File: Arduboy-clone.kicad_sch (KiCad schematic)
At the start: 0 parts

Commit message: Added MPU, Display and Decoupling Capacitors
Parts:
- added C? (x6): 0.1uF, Capacitor_SMD:C_0201_0603Metric, symbol PCM_SparkFun-Capacitor:0.1uF_0402_16V_10%
- added C? (x2): 22pF, PCM_SparkFun-Capacitor:C_0603_1608Metric, symbol PCM_SparkFun-Capacitor:C
- added C? (x2): 4.7uF, Capacitor_SMD:C_0201_0603Metric, symbol PCM_SparkFun-Capacitor:0.1uF_0402_16V_10%
- added C? (x3): 1uF, Capacitor_SMD:C_0201_0603Metric, symbol PCM_SparkFun-Capacitor:0.1uF_0402_16V_10%
- added R? (x2): 22k, PCM_SparkFun-Resistor:R_0402_1005Metric, symbol PCM_SparkFun-Resistor:22k_0402
- added R? (x2): 10k, PCM_SparkFun-Resistor:R_0402_1005Metric, symbol PCM_SparkFun-Resistor:10k_0402
- added SW? (x6): SW_Push, symbol Switch:SW_Push
- added U1: ATmega32U4-A, Package_QFP:TQFP-44_10x10mm_P0.8mm, symbol MCU_Microchip_ATmega:ATmega32U4-A
- added U?: OLED_1.3in, PCM_SparkFun-Display:OLED_1.3in_128x64-Folded, symbol PCM_SparkFun-Display:OLED_1.3in
- added Y1: 16MHz, PCM_SparkFun-Clock:Crystal_SMD_2.0x1.6mm, symbol PCM_SparkFun-Clock:Crystal_16MHz_2.0x1.6mm
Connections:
- new net: C?.1, U?.2 (C2P)
- new net: C?.1, U?.27 (VCOMH)
- new net: C?.1, U?.28 (VCC)
- new net: C?.2, U?.3 (C2N)
- new net: C?.2, U?.4 (C1P)
- new net: C?.1, U?.5 (C1N)
- new net: SW?.1, U1.39 (PF4)
- new net: R?.2, U1.4 (D+)
- new net: R?.1, U1.33 (~{HWB}/PE2)
- new net: C?.1, U1.16 (XTAL2), Y1.1
- new net: SW?.1, U1.36 (PF7)
- new net: C?.2, U1.6 (UCAP)
- new net: SW?.1, U1.1 (PE6)
- new net: SW?.1, U1.37 (PF6)
- new net: C?.2, U1.17 (XTAL1), Y1.2
- new net: SW?.1, U1.28 (PB4)
- new net: R?.2, U1.3 (D-)
- new net: SW?.1, U1.38 (PF5)
- new net 5V: C?.1, C?.1, C?.1, C?.1, C?.1, C?.1, U1.14 (VCC), U1.2 (UVCC), U1.24 (AVCC), U1.34 (VCC), U1.44 (AVCC), U?.6 (VDDB), U?.9 (VDD)
- new net CLK: U1.9 (PB1), U?.18 (D0/SCK/SCL)
- new net CS: U1.27 (PD7), U?.13 (~{CS})
- new net DC: U1.25 (PD4), U?.15 (D/~{C})
- new net GND: C?.1, C?.1, C?.2, C?.2, C?.2, C?.2, C?.2, C?.2, C?.2, C?.2, C?.2, R?.2, R?.2, SW?.2, SW?.2, SW?.2, SW?.2, SW?.2, SW?.2, U1.15 (GND), U1.23 (GND), U1.35 (GND), U1.43 (GND), U1.5 (UGND), U?.1 (GND), U?.10 (BS0), U?.11 (BS1), U?.12 (BS2), U?.16 (R/~{W}), U?.17 (E/~{RD}), U?.20 (D2/SDA), U?.21 (D3), U?.22 (D4), U?.23 (D5), U?.24 (D6), U?.29 (VLSS), U?.30 (GND), U?.8 (VSS)
- new net MOSI: U1.10 (PB2), U?.19 (D1/MOSI/SDA)
- new net RES: U1.31 (PC6), U?.14 (~{RESET})
- new net RESET: R?.1, U1.13 (~{RESET})
- new net USB_D+: R?.1
- new net USB_D-: R?.1

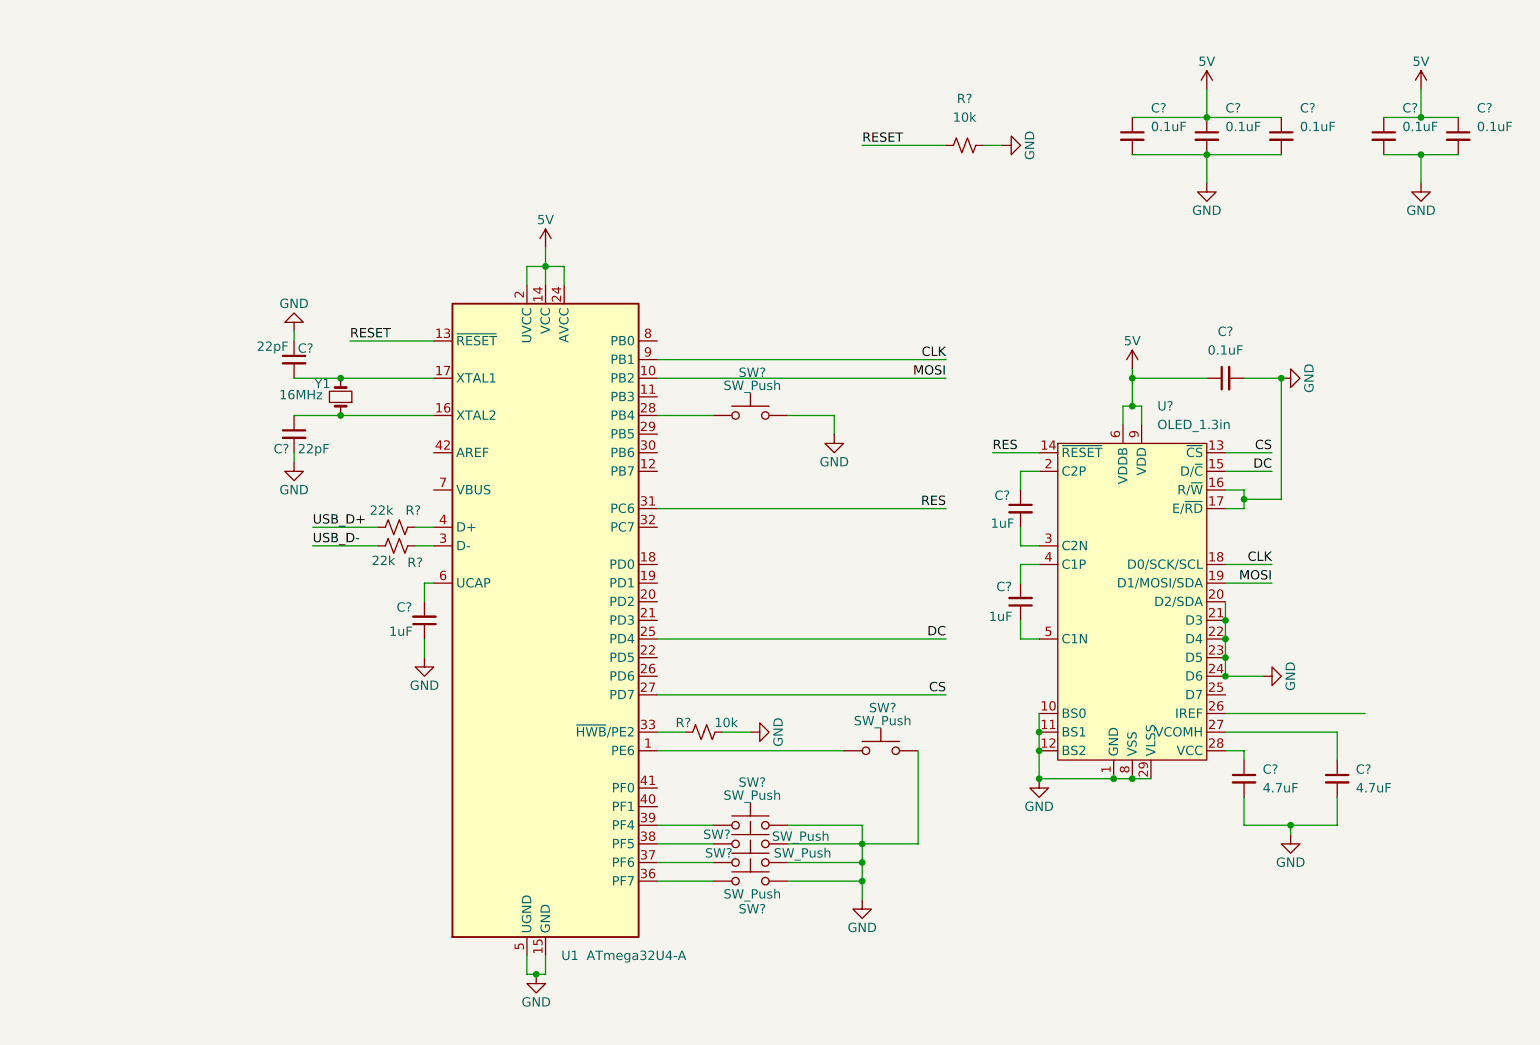
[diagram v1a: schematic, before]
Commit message: added display header
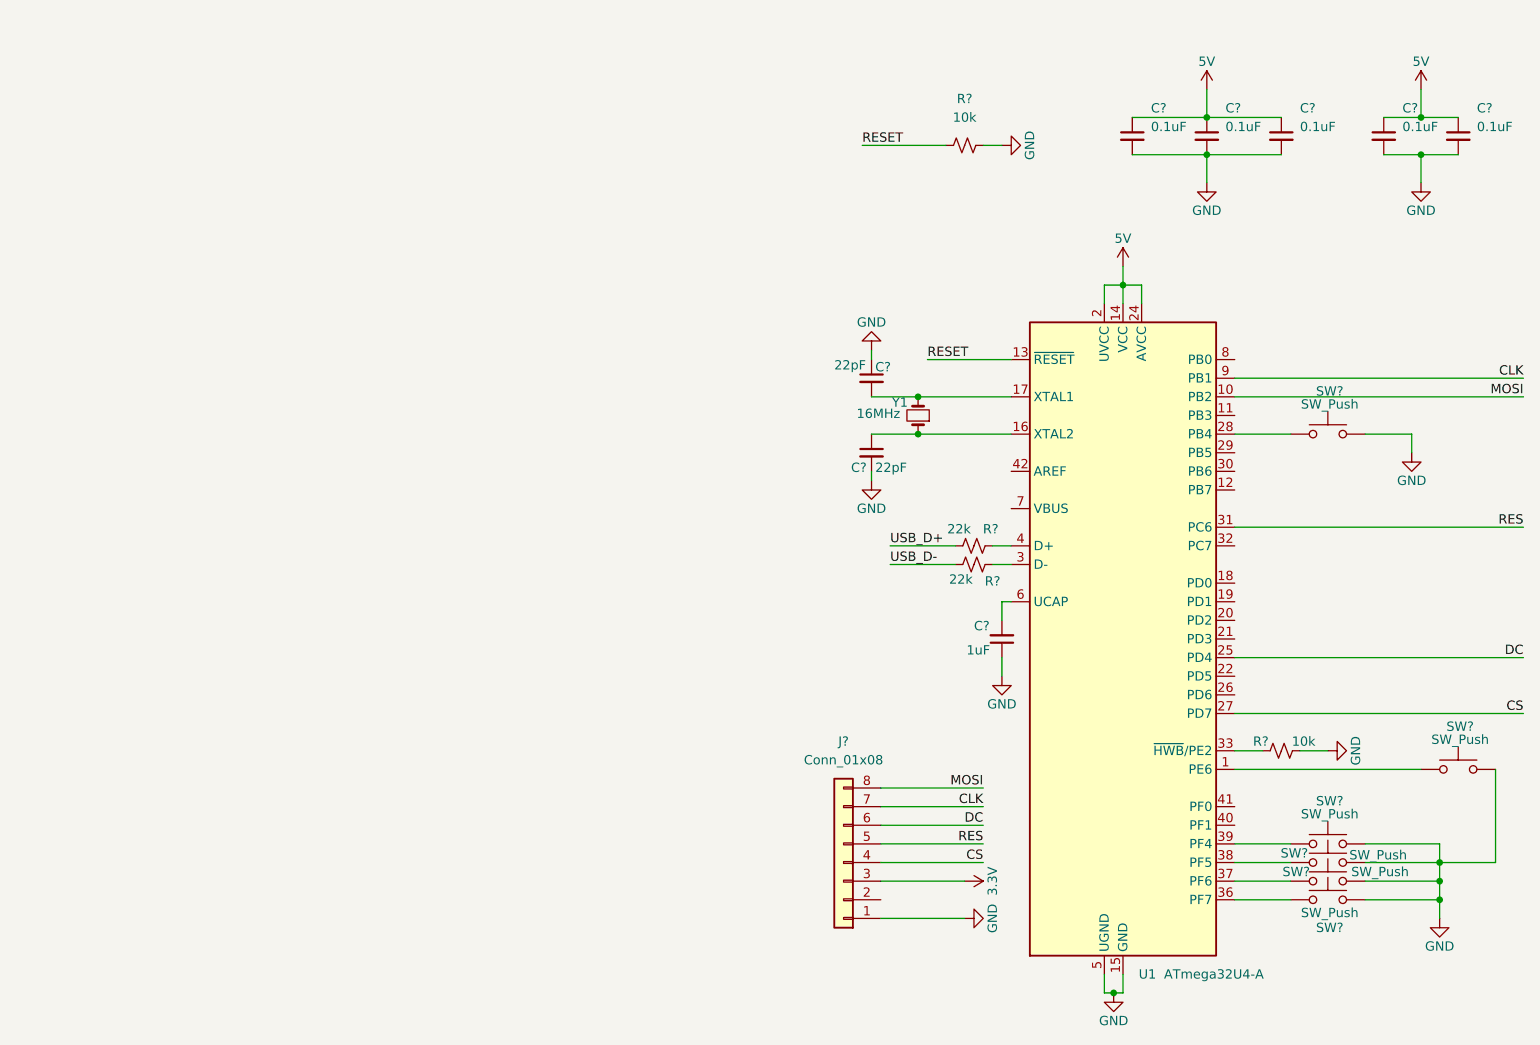
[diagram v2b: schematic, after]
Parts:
- removed C? (x2): 4.7uF, Capacitor_SMD:C_0201_0603Metric, symbol PCM_SparkFun-Capacitor:0.1uF_0402_16V_10%
- removed C?: 0.1uF, Capacitor_SMD:C_0201_0603Metric, symbol PCM_SparkFun-Capacitor:0.1uF_0402_16V_10%
- removed C? (x2): 1uF, Capacitor_SMD:C_0201_0603Metric, symbol PCM_SparkFun-Capacitor:0.1uF_0402_16V_10%
- removed U?: OLED_1.3in, PCM_SparkFun-Display:OLED_1.3in_128x64-Folded, symbol PCM_SparkFun-Display:OLED_1.3in
- added J?: Conn_01x08, symbol Connector_Generic:Conn_01x08
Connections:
- net CLK: now also J?.7 (Pin_7)
- net CS: now also J?.4 (Pin_4)
- net DC: now also J?.6 (Pin_6)
- net GND: now also J?.1 (Pin_1)
- net MOSI: now also J?.8 (Pin_8)
- net RES: now also J?.5 (Pin_5)
- new net 3.3V: J?.3 (Pin_3)
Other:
- moved on the sheet: C?, R?, SW?, U1, Y1

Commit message: added power circuit, display, USB-C circuits
I added the rest of the circuit and completed the whole schematic
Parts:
- added BT1: 3x AAA, Battery:BatteryHolder_Keystone_2479_3xAAA, symbol Device:Battery
- added BZ1: Buzzer, Buzzer_Beeper:Buzzer_Murata_PKLCS1212E, symbol Device:Buzzer
- added C1: 4.7uF, PCM_SparkFun-Capacitor:C_0603_1608Metric, symbol PCM_SparkFun-Capacitor:C
- added C2: 10uF, PCM_SparkFun-Capacitor:C_0603_1608Metric, symbol PCM_SparkFun-Capacitor:C
- added D1, D2: 1N5819WS, Diode_SMD:D_SOD-323, symbol Diode:1N5819WS
- added J1: USB_C_Receptacle_USB2.0_16P, Connector_USB:USB_C_Receptacle_HCTL_HC-TYPE-C-16P-01A, symbol Connector:USB_C_Receptacle_USB2.0_16P
- added L1: 4.7uH, PCM_SparkFun-Coil:1008_2520Metric, symbol PCM_SparkFun-Coil:4.7uH_1008_1.4A
- added R1: 309K, Capacitor_SMD:C_0603_1608Metric, symbol Device:R
- added R2, R3: 5.1K, Capacitor_SMD:C_0402_1005Metric, symbol Device:R
- added R4: 976K, Capacitor_SMD:C_0603_1608Metric, symbol Device:R
- added SW7: SW_Push, Button_Switch_THT:SW_PUSH_6mm, symbol Switch:SW_Push
- added U2: MCP1640Cx-xCHY, Package_TO_SOT_SMD:SOT-23-6, symbol Regulator_Switching:MCP1640Cx-xCHY
- J2: renamed from J?; footprint (none) -> Display:Adafruit_SSD1306
- SW1, SW2, SW3, SW4, SW5, SW6: renamed from SW?; footprint (none) -> Button_Switch_THT:SW_PUSH_6mm
- gave numbers to parts that had none: 12
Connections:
- net 3.3V is gone; now on net 5V: J2.3 (Pin_3)
- net 5V: now also D1.1 (K), D2.1 (K)
- net CS: now also U1.26 (PD6); no longer U1.27 (PD7)
- net GND: now also BT1.2 (-), C1.2, C2.2, J1.A1 (GND), J1.A12 (GND), J1.B1 (GND), J1.B12 (GND), J1.S1 (SHIELD), R1.2, R2.1, R3.2, U2.2 (GND)
- net RES: now also U1.27 (PD7); no longer U1.31 (PC6)
- net RESET: now also SW7.1; no longer U1.13 (~{RESET})
- net USB_D+: now also J1.A6 (D+), J1.B6 (D+)
- net USB_D-: now also J1.A7 (D-), J1.B7 (D-)
- net at U1.32 (PC7): now also BZ1.2 (-)
- new net: L1.2, U2.1 (SW)
- new net: BT1.1 (+), C1.1, L1.1, U2.3 (EN), U2.6 (V_{IN})
- new net: R1.1, R4.2, U2.4 (V_{FB})
- new net: C2.1, D2.2 (A), R4.1, U2.5 (V_{OUT})
- new net: J1.A5 (CC1), R2.2
- new net: D1.2 (A), J1.A4 (VBUS), J1.A9 (VBUS), J1.B4 (VBUS), J1.B9 (VBUS)
- new net: J1.B5 (CC2), R3.1
- new net: SW7.2, U1.13 (~{RESET})
- new net: BZ1.1 (+), U1.31 (PC6)
- no-connect marks 0 -> 2
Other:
- moved on the sheet: C3, C4, J2

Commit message: Completely routed the board
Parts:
- BT1: footprint Battery:BatteryHolder_Keystone_2479_3xAAA -> Battery:BatteryHolder_Keystone_2468_2xAAA
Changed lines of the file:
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@@
 			)
 		)
-		(property "Footprint" "Battery:BatteryHolder_Keystone_2479_3xAAA"
+		(property "Footprint" "Battery:BatteryHolder_Keystone_2468_2xAAA"
 			(at 97.536 52.07 90)
 			(effects

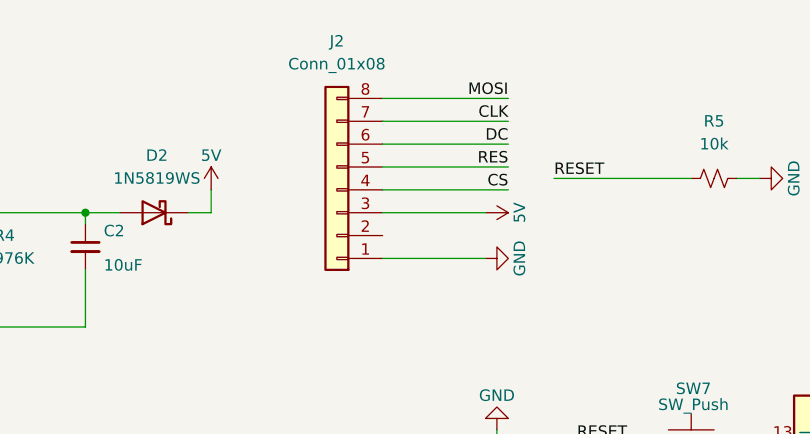
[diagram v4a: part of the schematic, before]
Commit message: Added Bom file and replaced display with a cheaper alternative
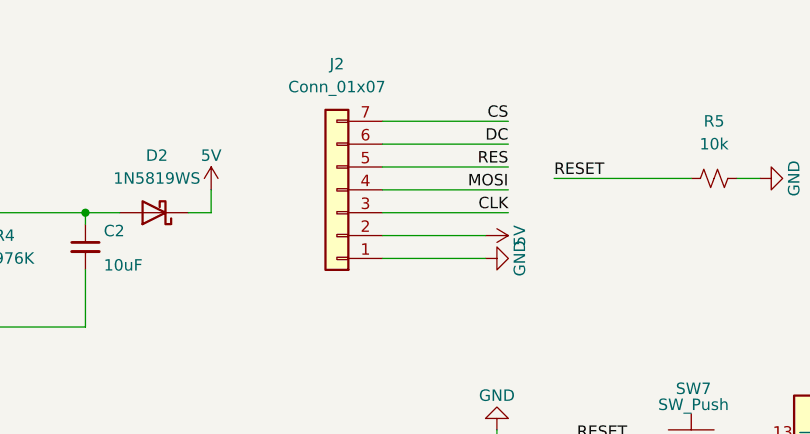
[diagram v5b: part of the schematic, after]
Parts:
- removed J2: Conn_01x08, Display:Adafruit_SSD1306, symbol Connector_Generic:Conn_01x08
- added J2: Conn_01x07, Connector_PinHeader_2.54mm:PinHeader_1x07_P2.54mm_Vertical, symbol Connector_Generic:Conn_01x07
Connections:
- net 5V: now also J2.2 (Pin_2)
- net CLK: now also J2.3 (Pin_3)
- net CS: now also J2.7 (Pin_7)
- net DC: now also J2.6 (Pin_6)
- net GND: now also J2.1 (Pin_1)
- net MOSI: now also J2.4 (Pin_4)
- net RES: now also J2.5 (Pin_5)
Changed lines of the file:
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@@
 	(wire
 		(pts
-			(xy 163.83 26.67) (xy 177.8 26.67)
+			(xy 163.83 36.83) (xy 177.8 36.83)
 		)
 		(stroke
@@
 	(wire
 		(pts
-			(xy 163.83 36.83) (xy 175.26 36.83)
+			(xy 163.83 39.37) (xy 175.26 39.37)
 		)
 		(stroke
@@
 	(wire
 		(pts
-			(xy 163.83 34.29) (xy 177.8 34.29)
+			(xy 163.83 26.67) (xy 177.8 26.67)
 		)
 		(stroke
@@
 	(wire
 		(pts
-			(xy 163.83 24.13) (xy 177.8 24.13)
+			(xy 163.83 34.29) (xy 177.8 34.29)
 		)
 		(stroke
@@
 	)
 	(label "CLK"
-		(at 177.8 26.67 180)
+		(at 177.8 36.83 180)
 		(effects
 			(font
@@
 	)
 	(label "CS"
-		(at 177.8 34.29 180)
+		(at 177.8 26.67 180)
 		(effects
 			(font
@@
 	)
 	(label "MOSI"
-		(at 177.8 24.13 180)
+		(at 177.8 34.29 180)
 		(effects
 			(font
@@
 	)
 	(symbol
-		(lib_id "Connector_Generic:Conn_01x08")
-		(at 158.75 34.29 180)
-		(unit 1)
-		(exclude_from_sim no)
-		(in_bom yes)
-		(on_board yes)
-		(dnp no)
-		(fields_autoplaced yes)
-		(property "Reference" "J2"
-			(at 158.75 17.78 0)
-			(effects
-				(font
-					(size 1.27 1.27)
-				)
-			)
-		)
-		(property "Value" "Conn_01x08"
-			(at 158.75 20.32 0)
-			(effects
-				(font
-					(size 1.27 1.27)
-				)
-			)
-		)
-		(property "Footprint" "Display:Adafruit_SSD1306"
-			(at 158.75 34.29 0)
-			(effects
-				(font
-					(size 1.27 1.27)
-				)
-				(hide yes)
-			)
-		)
-		(property "Datasheet" "~"
-			(at 158.75 34.29 0)
-			(effects
-				(font
-					(size 1.27 1.27)
-				)
-				(hide yes)
-			)
-		)
-		(property "Description" "Generic connector, single row, 01x08, script generated (kicad-library-utils/schlib/autogen/connector/)"
-			(at 158.75 34.29 0)
-			(effects
-				(font
-					(size 1.27 1.27)
-				)
-				(hide yes)
-			)
-		)
-		(pin "1"
-		)
-		(pin "6"
-		)
-		(pin "2"
-		)
-		(pin "4"
-		)
-		(pin "5"
-		)
-		(pin "3"
-		)
-		(pin "7"
-		)
-		(pin "8"
-		)
-		(instances
-			(project ""
-				(path "/5af127a6-c873-46d1-bf24-0405669f4d95"
-					(reference "J2")
-					(unit 1)
-				)
-			)
-		)
-	)
-	(symbol
 		(lib_id "PCM_SparkFun-PowerSymbol:5V")
-		(at 175.26 36.83 270)
+		(at 175.26 39.37 270)
 		(unit 1)
 		(exclude_from_sim no)
@@
 		(fields_autoplaced yes)
 		(property "Reference" "#PWR014"
-			(at 171.45 36.83 0)
+			(at 171.45 39.37 0)
 			(effects
 				(font
@@
 		)
 		(property "Value" "5V"
-			(at 179.07 36.83 0)
+			(at 179.07 39.37 0)
 			(do_not_autoplace yes)
 			(effects
@@
 		)
 		(property "Footprint" ""
-			(at 175.26 36.83 0)
+			(at 175.26 39.37 0)
 			(effects
 				(font
@@
 		)
 		(property "Datasheet" ""
-			(at 175.26 36.83 0)
+			(at 175.26 39.37 0)
 			(effects
 				(font
@@
 		)
 		(property "Description" "Power symbol creates a global label with name \"5V\""
-			(at 168.91 36.83 0)
+			(at 168.91 39.37 0)
 			(effects
 				(font
@@
 					(unit 1)
 				)
+			)
+		)
+	)
+	(symbol
+		(lib_id "Connector_Generic:Conn_01x07")
+		(at 158.75 34.29 180)
+		(unit 1)
+		(exclude_from_sim no)
+		(in_bom yes)
+		(on_board yes)
+		(dnp no)
+		(fields_autoplaced yes)
+		(property "Reference" "J2"
+			(at 158.75 20.32 0)
+			(effects
+				(font
+					(size 1.27 1.27)
+				)
+			)
+		)
+		(property "Value" "Conn_01x07"
+			(at 158.75 22.86 0)
+			(effects
+				(font
+					(size 1.27 1.27)
+				)
+			)
+		)
+		(property "Footprint" "Connector_PinHeader_2.54mm:PinHeader_1x07_P2.54mm_Vertical"
+			(at 158.75 34.29 0)
+			(effects
+				(font
+					(size 1.27 1.27)
+				)
+				(hide yes)
+			)
+		)
+		(property "Datasheet" "~"
+			(at 158.75 34.29 0)
+			(effects
+				(font
+					(size 1.27 1.27)
+				)
+				(hide yes)
+			)
+		)
+		(property "Description" "Generic connector, single row, 01x07, script generated (kicad-library-utils/schlib/autogen/connector/)"
+			(at 158.75 34.29 0)
+			(effects
+				(font
+					(size 1.27 1.27)
+				)
+				(hide yes)
+			)
+		)
+		(pin "4"
+		)
+		(pin "5"
+		)
+		(pin "6"
+		)
+		(pin "3"
+		)
+		(pin "2"
+		)
+		(pin "7"
+		)
+		(pin "1"
+		)
+		(instances
+			(project ""
+				(path "/5af127a6-c873-46d1-bf24-0405669f4d95"
+					(reference "J2")
+					(unit 1)
+				)
